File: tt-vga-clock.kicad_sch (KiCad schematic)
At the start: 47 parts, among them J2 Conn_01x02, J3 Conn_02x04_Odd_Even, J4 Conn_01x06, J6 Conn_02x18_Odd_Even, J6 USB_C_Receptacle_USB2.0, J9 613012243121, SW3 B3U-1000P, U1 Caravel_QFN, U1 W25Q32JVSS, X1 10MHz

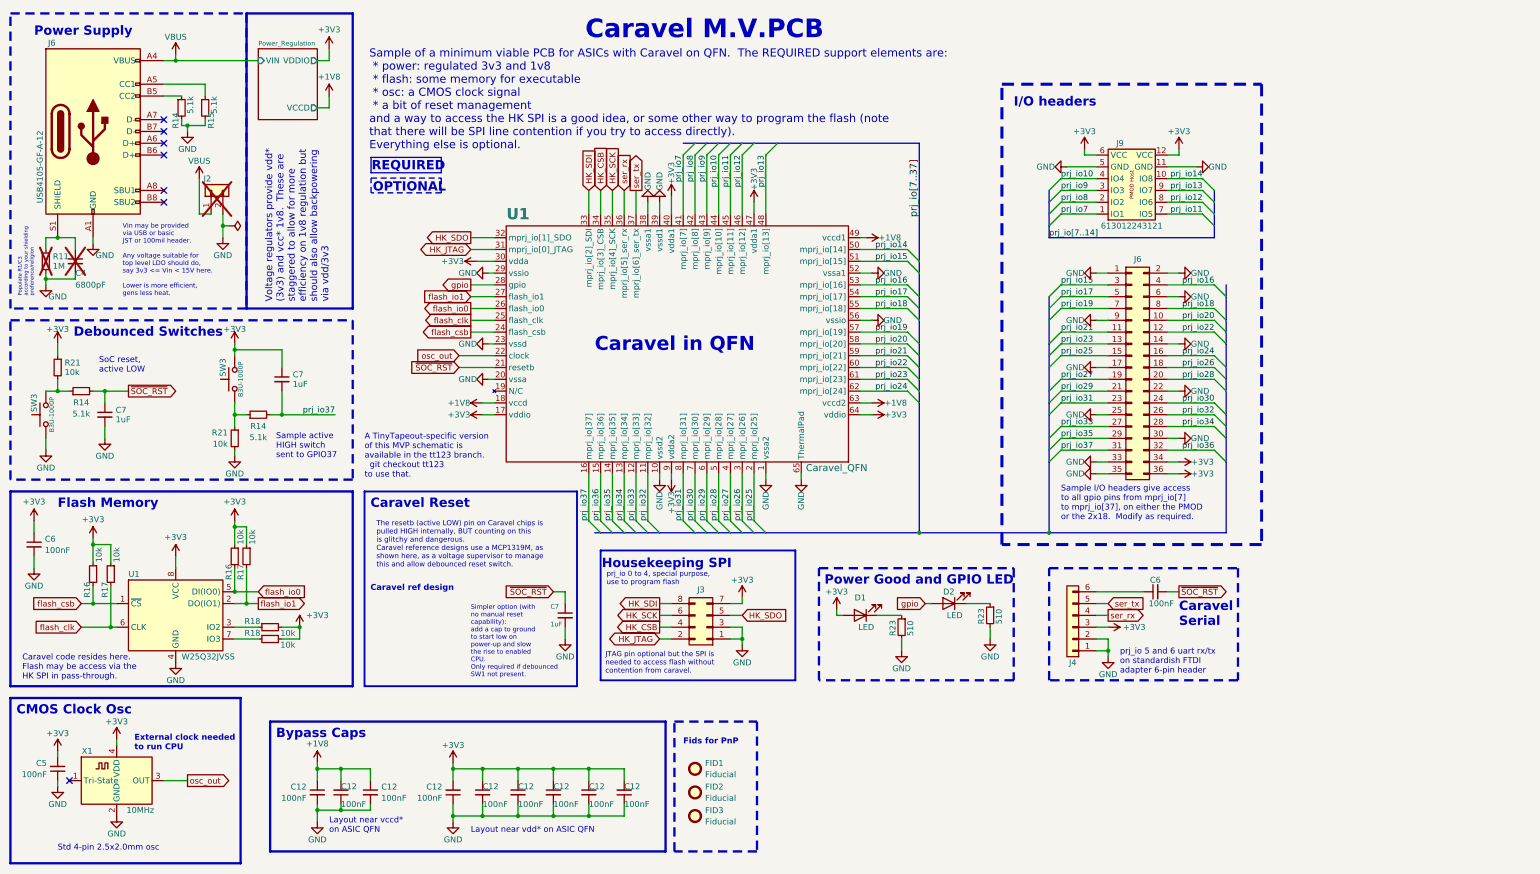
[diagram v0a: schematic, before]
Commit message: pinout for buttons, delete unneeded parts
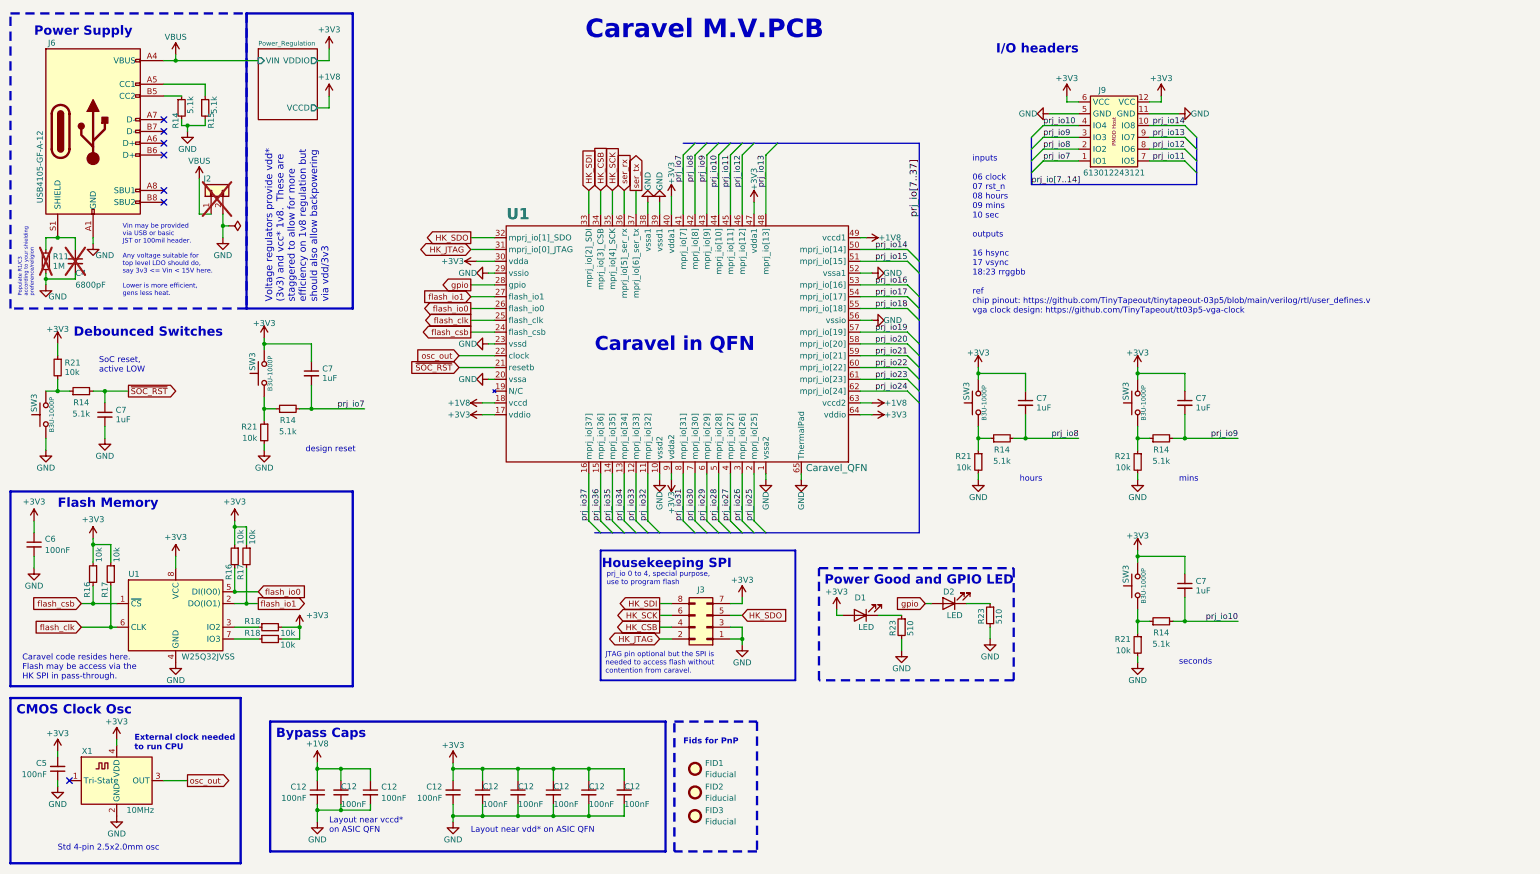
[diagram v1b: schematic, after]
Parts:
- removed C6: 100nF, Capacitor_SMD:C_0603_1608Metric, symbol Device:C_Small
- removed C7: 1uF, Capacitor_SMD:C_0603_1608Metric, symbol Device:C_Small
- removed J4: Conn_01x06, Connector_PinHeader_2.54mm:PinHeader_1x06_P2.54mm_Vertical, symbol Connector_Generic:Conn_01x06
- removed J6: Conn_02x18_Odd_Even, Connector_PinHeader_2.54mm:PinHeader_2x18_P2.54mm_Vertical, symbol Connector_Generic:Conn_02x18_Odd_Even
- added C7 (x3): 1uF, Capacitor_SMD:C_0603_1608Metric, symbol Device:C_Small
- added R14 (x3): 5.1k, Resistor_SMD:R_0603_1608Metric, symbol Device:R_Small
- added R21 (x3): 10k, Resistor_SMD:R_0603_1608Metric, symbol Device:R_Small
- added SW3 (x3): B3U-1000P, Button_Switch_SMD:SW_SPST_B3U-1000P, symbol Switch:SW_Push
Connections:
- net +3V3: now also C7.1, C7.1, C7.1, SW3.2, SW3.2, SW3.2
- net GND: now also R21.2, R21.2, R21.2
- net prj_io10: now also C7.2, R14.2
- net prj_io37: no longer C7.2, R14.2
- net prj_io7: now also C7.2, R14.2
- net prj_io8: now also C7.2, R14.2
- net prj_io9: now also C7.2, R14.2
- new net: R14.1, R21.1, SW3.1 (x3)
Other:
- note added: "design reset"
- note added: "hours"
- note added: "inputs 06 clock 07 rst_n 08 hours 09 mins 10 sec outputs 16 hsync 17 vsync 18:23 rrggbb ref chip pinout: https://github.com/TinyTapeout/tinytapeout-03p5/blob/main/verilog/rtl/user_defines.v vga clock design: https://github.com/TinyTapeout/tt03p5-vga-clock"
- note added: "mins"
- note added: "seconds"
- note removed: "A TinyTapeout-specific version of this MVP schematic is available in the tt123 branch. git checkout tt123 to use that."
- note removed: "Caravel Reset"
- note removed: "Caravel Serial"
- note removed: "Caravel ref design"
- note removed: "OPTIONAL"
- note removed: "REQUIRED"
- note removed: "Sample I/O headers give access to all gpio pins from mprj_io[7] to mprj_io[37], on either the PMOD or the 2x18. Modify as required."
- note removed: "Sample active HIGH switch sent to GPIO37"
- note removed: "Sample of a minimum viable PCB for ASICs with Caravel on QFN. The REQUIRED support elements are: * power: regulated 3v3 and 1v8 * flash: some memory for executable * osc: a CMOS clock signal * a bit of reset management and a way to access the HK SPI is a good idea, or some other way to program the flash (note that there will be SPI line contention if you try to access directly). Everything else i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"
- note removed: "Simpler option (with no manual reset capability): add a cap to ground to start low on power-up and slow the rise to enabled CPU. Only required if debounced SW1 not present."
- note removed: "The resetb (active LOW) pin on Caravel chips is pulled HIGH internally, BUT counting on this is glitchy and dangerous. Caravel reference designs use a MCP1319M, as shown here, as a voltage supervisor to manage this and allow debounced reset switch."
- note removed: "prj_io 5 and 6 uart rx/tx on standardish FTDI adapter 6-pin header"
- moved on the sheet: C7, J9, R14, R21, SW3

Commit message: schematic done
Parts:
- removed J2: Conn_01x02, Connector_JST:JST_PH_B2B-PH-K_1x02_P2.00mm_Vertical, symbol Connector_Generic:Conn_01x02
- removed J9: 613012243121, TinyTapeout:PinSocket_2x06_P2.54mm_PMODHost1A, symbol TinyTapeout:PMOD_HOST_2x6
- added C7: 1uF, Capacitor_SMD:C_0603_1608Metric, symbol Device:C_Small
- added J5: DE15_Receptacle_HighDensity_MountingHoles, Connector_Dsub:DSUB-15-HD_Female_Horizontal_P2.29x1.98mm_EdgePinOffset8.35mm_Housed_MountingHolesOffset10.89mm, symbol Connector:DE15_Receptacle_HighDensity_MountingHoles
- added NT1, NT2: NetTie_2, NetTie:NetTie-2_SMD_Pad0.5mm, symbol Device:NetTie_2
- added R14 (x3): 500R, Resistor_SMD:R_0603_1608Metric, symbol Device:R_Small
- added R14 (x3): 1k, Resistor_SMD:R_0603_1608Metric, symbol Device:R_Small
- added TP1, TP2: TestPoint, TestPoint:TestPoint_Pad_1.0x1.0mm, symbol Connector:TestPoint
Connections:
- net GND: now also C7.2, J5.10, J5.5, J5.6, J5.7, J5.8
- net prj_io16: now also NT1.1
- net prj_io17: now also NT2.1
- net prj_io18: now also R14.1
- net prj_io19: now also R14.1
- net prj_io20: now also R14.1
- net prj_io21: now also R14.1
- net prj_io22: now also R14.1
- net prj_io23: now also R14.1
- net ~{SOC_RST}: now also C7.1
- new net blue: J5.3, R14.2, R14.2
- new net green: J5.2, R14.2, R14.2
- new net hsync: J5.13, NT1.2, TP1.1
- new net red: J5.1, R14.2, R14.2
- new net vsync: J5.14, NT2.2, TP2.1
- no-connect marks 7 -> 13
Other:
- note added: "I/O"
- note added: "SoC Caravel reset"
- note added: "TT3p5 VGA Clock PCB"
- note added: "inputs 06 clock 07 rst_n 08 hours 09 mins 10 sec outputs 16 hsync 17 vsync 18:23 rrggbb"
- note added: "ref chip pinout: https://github.com/TinyTapeout/tinytapeout-03p5/blob/main/verilog/rtl/user_defines.v vga clock design: https://github.com/TinyTapeout/tt03p5-vga-clock"
- note removed: "Caravel M.V.PCB"
- note removed: "I/O headers"
- note removed: "Vin may be provided via USB or basic JST or 100mil header. Any voltage suitable for top level LDO should do, say 3v3 <= Vin < 15V here. Lower is more efficient, gens less heat."
- note removed: "inputs 06 clock 07 rst_n 08 hours 09 mins 10 sec outputs 16 hsync 17 vsync 18:23 rrggbb ref chip pinout: https://github.com/TinyTapeout/tinytapeout-03p5/blob/main/verilog/rtl/user_defines.v vga clock design: https://github.com/TinyTapeout/tt03p5-vga-clock"
- moved on the sheet: C7, D1, D2, J3, R14, R21, R23, SW3

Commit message: start layout
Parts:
- removed C12 (x5): 100nF, Capacitor_SMD:C_0603_1608Metric, symbol Device:C_Small
- removed C4: 6800pF, Capacitor_SMD:C_0603_1608Metric, symbol Device:C_Small
- removed C7: 1uF, Capacitor_SMD:C_0603_1608Metric, symbol Device:C_Small
- removed R14: 5.1k, Resistor_SMD:R_0603_1608Metric, symbol Device:R_Small
- removed R21: 10k, Resistor_SMD:R_0603_1608Metric, symbol Device:R_Small
- removed SW3: B3U-1000P, Button_Switch_SMD:SW_SPST_B3U-1000P, symbol Switch:SW_Push
- added NT3: NetTie_2, NetTie:NetTie-2_SMD_Pad0.5mm, symbol Device:NetTie_2
- added TP3: TestPoint, TestPoint:TestPoint_Pad_1.0x1.0mm, symbol Connector:TestPoint
- R11: now fitted
- X1: value 10MHz -> 31.5MHz
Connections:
- net osc_out: now also NT3.1
- net ser_tx: now also NT3.2
- net ~{SOC_RST}: now also TP3.1
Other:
- note removed: "Debounced Switches"
- note removed: "Populate R1/C3 according to your shielding preference/religion"
- note removed: "SoC reset, active LOW"

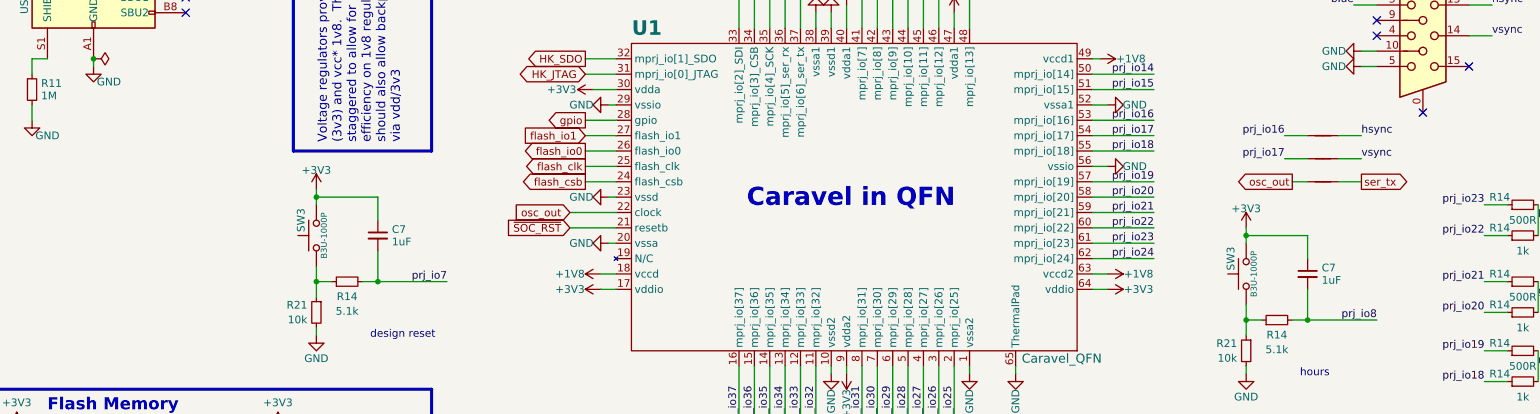
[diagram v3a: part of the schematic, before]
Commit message: oshw mark, better silk, edge cuts, all nets connected
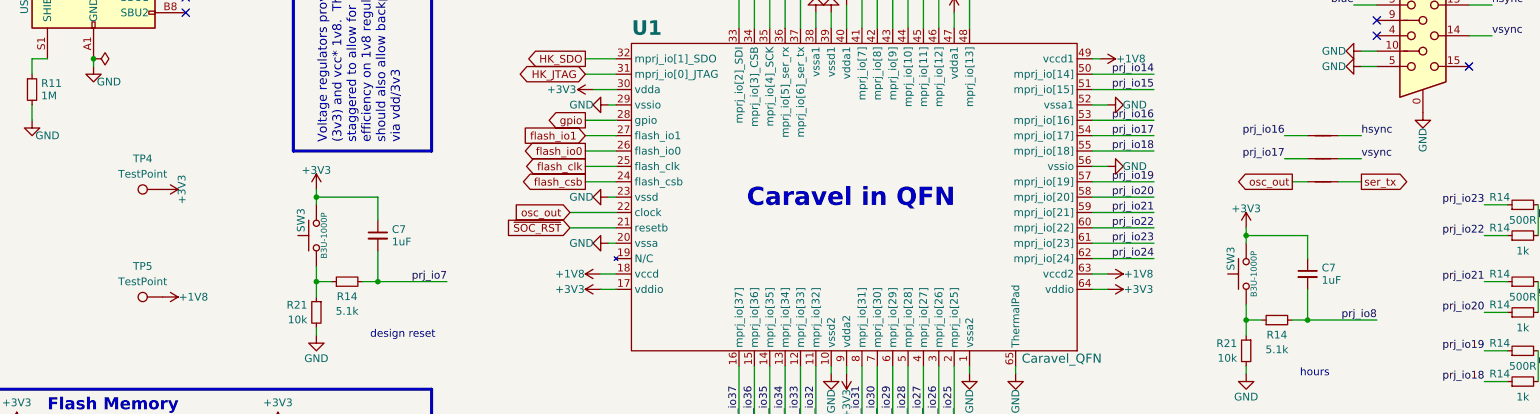
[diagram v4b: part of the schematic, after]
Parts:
- added TP4, TP5: TestPoint, TestPoint:TestPoint_Pad_1.0x1.0mm, symbol Connector:TestPoint
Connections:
- net +1V8: now also TP5.1
- net +3V3: now also TP4.1
- net GND: now also J5.0
- no-connect marks 13 -> 12
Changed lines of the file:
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@@
   (no_connect (at 45.72 43.18))
   (no_connect (at 25.4 177.8))
-  (no_connect (at 250.19 69.85))
   (no_connect (at 45.72 53.34))
   (no_connect (at 257.81 41.91))
@@
     )
   )
+  (symbol (lib_name "GND_1") (lib_id "power:GND") (at 250.19 69.85 0) (mirror y) (unit 1)
+    (in_bom yes) (on_board yes) (dnp no)
+    (property "Reference" "#PWR04" (at 250.19 76.2 0)
+      (effects (font (size 1.27 1.27)) hide)
+    )
+    (property "Value" "GND" (at 250.19 72.39 90)
+      (effects (font (size 1.27 1.27)) (justify right))
+    )
+    (property "Footprint" "" (at 250.19 69.85 0)
+      (effects (font (size 1.27 1.27)) hide)
+    )
+    (property "Datasheet" "" (at 250.19 69.85 0)
+      (effects (font (size 1.27 1.27)) hide)
+    )
+    (pin "1")
+    (instances
+      (project "tt-vga-clock"
+        (path "/d2f3109e-08ec-4d18-8cdf-c360e3b1458b"
+          (reference "#PWR04") (unit 1)
+        )
+      )
+    )
+  )
   (symbol (lib_id "Device:R_Small") (at 224.79 144.78 90) (unit 1)
     (in_bom yes) (on_board yes) (dnp no) (fields_autoplaced)
@@
     )
   )
+  (symbol (lib_id "Connector:TestPoint") (at 41.91 82.55 90) (unit 1)
+    (in_bom yes) (on_board yes) (dnp no) (fields_autoplaced)
+    (property "Reference" "TP4" (at 38.608 77.47 90)
+      (effects (font (size 1.27 1.27)))
+    )
+    (property "Value" "TestPoint" (at 38.608 80.01 90)
+      (effects (font (size 1.27 1.27)))
+    )
+    (property "Footprint" "TestPoint:TestPoint_Pad_1.0x1.0mm" (at 41.91 77.47 0)
+      (effects (font (size 1.27 1.27)) hide)
+    )
+    (property "Datasheet" "~" (at 41.91 77.47 0)
+      (effects (font (size 1.27 1.27)) hide)
+    )
+    (pin "1")
+    (instances
+      (project "tt-vga-clock"
+        (path "/d2f3109e-08ec-4d18-8cdf-c360e3b1458b"
+          (reference "TP4") (unit 1)
+        )
+      )
+    )
+  )
   (symbol (lib_id "power:+3V3") (at 35.56 168.91 0) (unit 1)
     (in_bom yes) (on_board yes) (dnp no)
@@
     )
   )
+  (symbol (lib_id "power:+1V8") (at 41.91 100.33 270) (mirror x) (unit 1)
+    (in_bom yes) (on_board yes) (dnp no)
+    (property "Reference" "#PWR010" (at 38.1 100.33 0)
+      (effects (font (size 1.27 1.27)) hide)
+    )
+    (property "Value" "+1V8" (at 46.99 100.33 90)
+      (effects (font (size 1.27 1.27)))
+    )
+    (property "Footprint" "" (at 41.91 100.33 0)
+      (effects (font (size 1.27 1.27)) hide)
+    )
+    (property "Datasheet" "" (at 41.91 100.33 0)
+      (effects (font (size 1.27 1.27)) hide)
+    )
+    (pin "1")
+    (instances
+      (project "tt-vga-clock"
+        (path "/d2f3109e-08ec-4d18-8cdf-c360e3b1458b"
+          (reference "#PWR010") (unit 1)
+        )
+      )
+    )
+  )
   (symbol (lib_id "power:GND") (at 35.56 185.42 0) (mirror y) (unit 1)
     (in_bom yes) (on_board yes) (dnp no)
@@
     )
   )
+  (symbol (lib_id "power:+3V3") (at 41.91 82.55 270) (unit 1)
+    (in_bom yes) (on_board yes) (dnp no)
+    (property "Reference" "#PWR05" (at 38.1 82.55 0)
+      (effects (font (size 1.27 1.27)) hide)
+    )
+    (property "Value" "+3V3" (at 45.085 82.55 0)
+      (effects (font (size 1.27 1.27)))
+    )
+    (property "Footprint" "" (at 41.91 82.55 0)
+      (effects (font (size 1.27 1.27)) hide)
+    )
+    (property "Datasheet" "" (at 41.91 82.55 0)
+      (effects (font (size 1.27 1.27)) hide)
+    )
+    (pin "1")
+    (instances
+      (project "tt-vga-clock"
+        (path "/d2f3109e-08ec-4d18-8cdf-c360e3b1458b"
+          (reference "#PWR05") (unit 1)
+        )
+      )
+    )
+  )
   (symbol (lib_name "GND_1") (lib_id "power:GND") (at 240.03 39.37 270) (mirror x) (unit 1)
     (in_bom yes) (on_board yes) (dnp no)
@@
         )
       )
+    )
+  )
+  (symbol (lib_id "Connector:TestPoint") (at 41.91 100.33 90) (unit 1)
+    (in_bom yes) (on_board yes) (dnp no) (fields_autoplaced)
+    (property "Reference" "TP5" (at 38.608 95.25 90)
+      (effects (font (size 1.27 1.27)))
+    )
+    (property "Value" "TestPoint" (at 38.608 97.79 90)
+      (effects (font (size 1.27 1.27)))
+    )
+    (property "Footprint" "TestPoint:TestPoint_Pad_1.0x1.0mm" (at 41.91 95.25 0)
+      (effects (font (size 1.27 1.27)) hide)
+    )
+    (property "Datasheet" "~" (at 41.91 95.25 0)
+      (effects (font (size 1.27 1.27)) hide)
+    )
+    (pin "1")
+    (instances
+      (project "tt-vga-clock"
+        (path "/d2f3109e-08ec-4d18-8cdf-c360e3b1458b"
+          (reference "TP5") (unit 1)
+        )
+      )

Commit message: use correct db15 fp
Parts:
- J5: footprint Connector_Dsub:DSUB-15-HD_Female_Horizontal_P2.29x1.98mm_EdgePinOffset8.35mm_Housed_MountingHolesOffset10.89mm -> footprints:db15
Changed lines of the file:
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@@
       (effects (font (size 1.27 1.27)))
     )
-    (property "Footprint" "Connector_Dsub:DSUB-15-HD_Female_Horizontal_P2.29x1.98mm_EdgePinOffset8.35mm_Housed_MountingHolesOffset10.89mm" (at 226.06 41.91 0)
+    (property "Footprint" "footprints:db15" (at 226.06 41.91 0)
       (effects (font (size 1.27 1.27)) hide)
     )
